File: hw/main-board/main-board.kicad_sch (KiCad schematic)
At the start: 26 parts, among them J1 USB_C_Receptacle_USB2.0_16P, Q1 AONR21307, U1 HUSB238_xxxDD, U2 AP63205WU, U3 AP2112K-3.3, U4 PTR54L, U5 TMC2226-SA

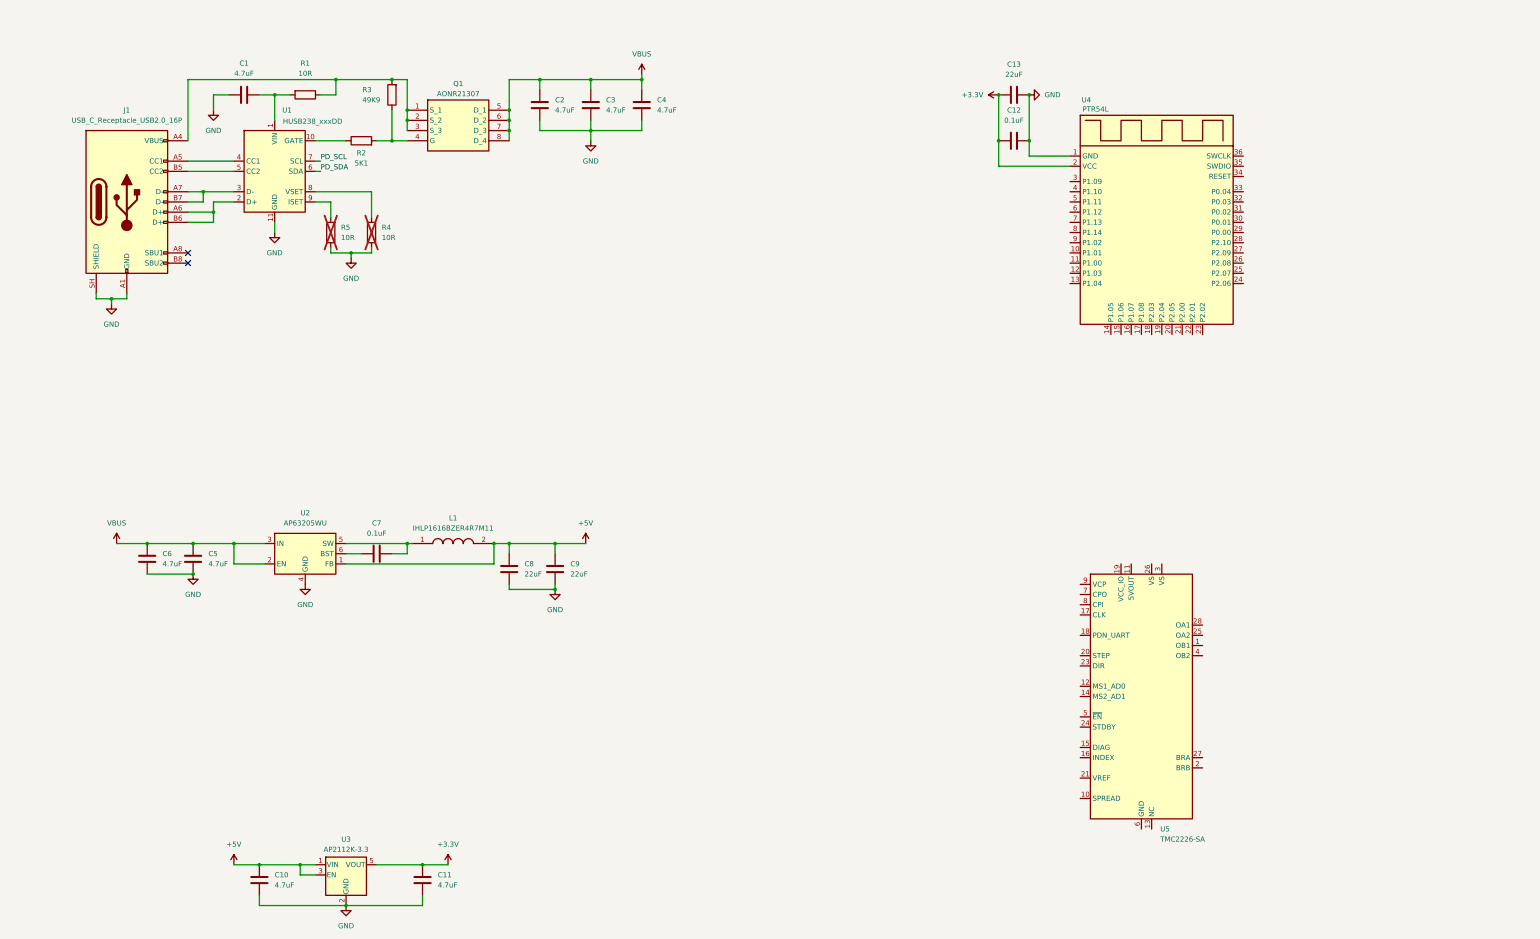
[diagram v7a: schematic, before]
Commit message: Add TMC2226 circuit
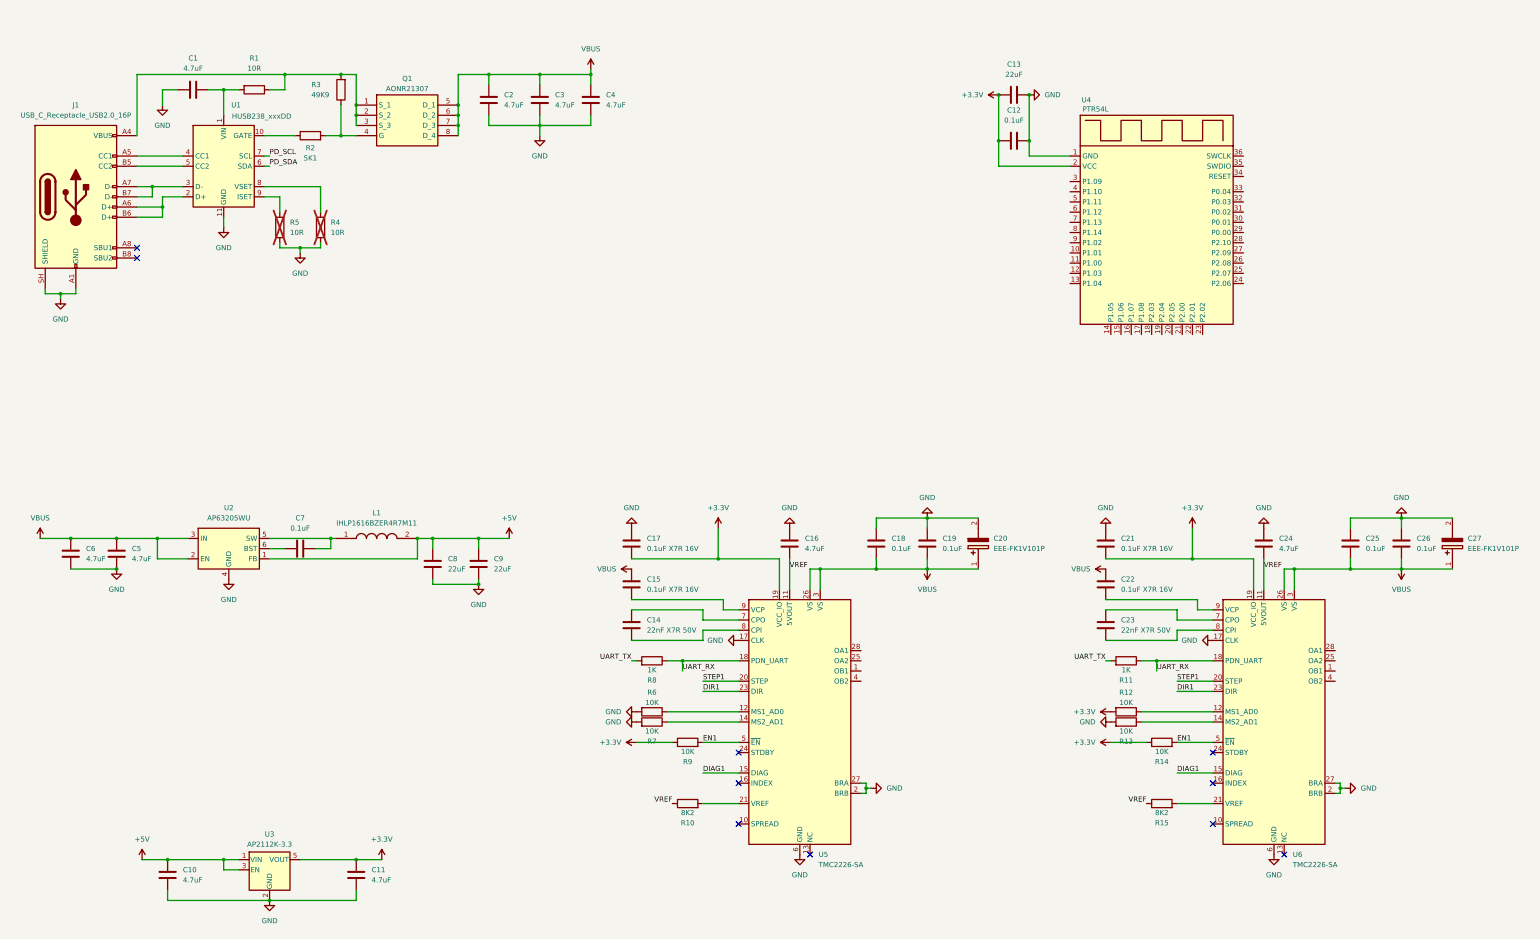
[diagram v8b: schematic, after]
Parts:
- added C14, C23: 22nF X7R 50V, Capacitor_SMD:C_0603_1608Metric_Pad1.08x0.95mm_HandSolder, symbol Device:C
- added C15, C17, C21, C22: 0.1uF X7R 16V, Capacitor_SMD:C_0603_1608Metric_Pad1.08x0.95mm_HandSolder, symbol Device:C
- added C16, C24: 4.7uF, Capacitor_SMD:C_0805_2012Metric_Pad1.18x1.45mm_HandSolder, symbol Device:C
- added C18, C19, C25, C26: 0.1uF, Capacitor_SMD:C_0805_2012Metric_Pad1.18x1.45mm_HandSolder, symbol Device:C
- added C20, C27: EEE-FK1V101P, EEHZT1E331UP, symbol Samacsys:EEE-FK1V101P
- added R10, R15: 8K2, Resistor_SMD:R_0603_1608Metric_Pad0.98x0.95mm_HandSolder, symbol Device:R
- added R11, R8: 1K, Resistor_SMD:R_0603_1608Metric_Pad0.98x0.95mm_HandSolder, symbol Device:R
- added R12, R13, R14, R6, R7, R9: 10K, Resistor_SMD:R_0603_1608Metric_Pad0.98x0.95mm_HandSolder, symbol Device:R
- added U6: TMC2226-SA, Package_SO:HTSSOP-28-1EP_4.4x9.7mm_P0.65mm_EP2.75x6.2mm_ThermalVias, symbol Driver_Motor:TMC2226-SA
- C10, C11, C12, C7: footprint Capacitor_SMD:C_0603_1608Metric_Pad1.08x0.95mm_HandSolder -> Capacitor_SMD:C_0805_2012Metric_Pad1.18x1.45mm_HandSolder
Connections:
- net +3.3V: now also U5.19 (VCC_IO), C17.2, C21.2, R12.2, R14.1, R9.1, U6.19 (VCC_IO)
- net GND: now also U5.17 (CLK), U5.2 (BRB), U5.22 (GND), U5.27 (BRA), U5.29 (GND), U5.6 (GND), C16.1, C17.1, C18.1, C19.1, C20.2 (-), C21.1, C24.1, C25.1, C26.1, C27.2 (-), R13.2, R6.2, R7.2, U6.17 (CLK), U6.2 (BRB), U6.22 (GND), U6.27 (BRA), U6.29 (GND), U6.6 (GND)
- net VBUS: now also U5.26 (VS), U5.3 (VS), C15.1, C18.2, C19.2, C20.1 (+), C22.1, C25.2, C26.2, C27.1 (+), U6.26 (VS), U6.3 (VS)
- net VREF: now reaches U5.11 (5VOUT)
- net VREF: now also C16.2, C24.2, R10.1, R15.1, U6.11 (5VOUT)
- net at U5.12 (MS1_AD0): now also R6.1
- net at U5.14 (MS2_AD1): now also R7.1
- net DIAG1: now reaches U5.15 (DIAG)
- net DIAG1: now also U6.15 (DIAG)
- net UART_RX: now reaches U5.18 (PDN_UART)
- net UART_RX: now also R11.1, R8.1, U6.18 (PDN_UART)
- net STEP1: now reaches U5.20 (STEP)
- net STEP1: now also U6.20 (STEP)
- net at U5.21 (VREF): now also R10.2
- net DIR1: now reaches U5.23 (DIR)
- net DIR1: now also U6.23 (DIR)
- net EN1: now reaches U5.5 (~{EN})
- net EN1: now also R14.2, R9.2, U6.5 (~{EN})
- net at U5.7 (CPO): now also C14.2
- net at U5.8 (CPI): now also C14.1
- net at U5.9 (VCP): now also C15.2
- new net: C23.1, U6.8 (CPI)
- new net: C23.2, U6.7 (CPO)
- new net: R12.1, U6.12 (MS1_AD0)
- new net: R13.1, U6.14 (MS2_AD1)
- new net: R15.2, U6.21 (VREF)
- new net: C22.2, U6.9 (VCP)
- new net UART_TX: R11.2, R8.2
- no-connect marks 2 -> 10
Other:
- moved on the sheet: C1, C10, C11, C2, C3, C4, C5, C6, C7, C8, C9, J1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
